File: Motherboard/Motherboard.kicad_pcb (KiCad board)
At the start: 2 copper layers, 75 x 75 mm, 43 parts, among them J1 AUX Analog A, J10 Moisture 4, J11 Moisture 5, J12 Power In, J2 AUX Analog B, J3 RPi 3B+, J4 AUX Digital A, J5 AUX Digital B, J6 Moisture 0, J7 Moisture 1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

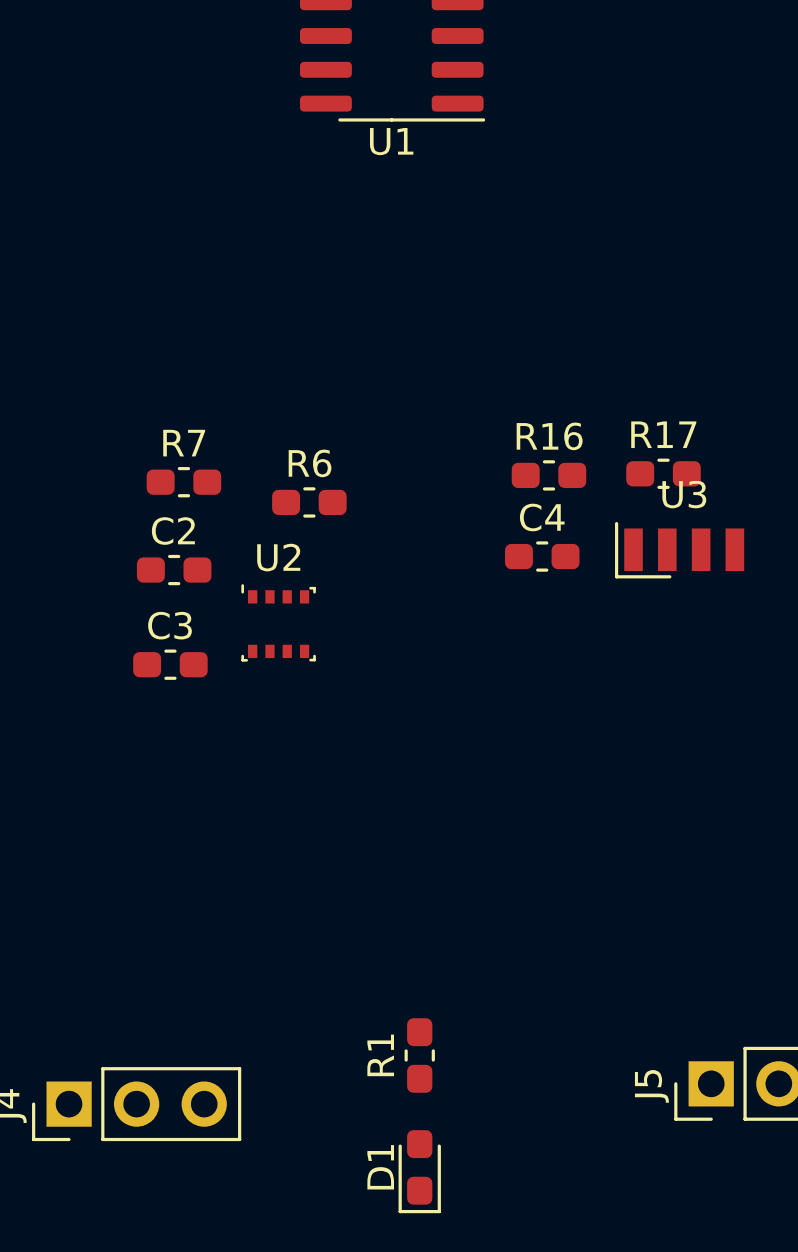
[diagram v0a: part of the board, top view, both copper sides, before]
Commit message: added missing footprint on new cap
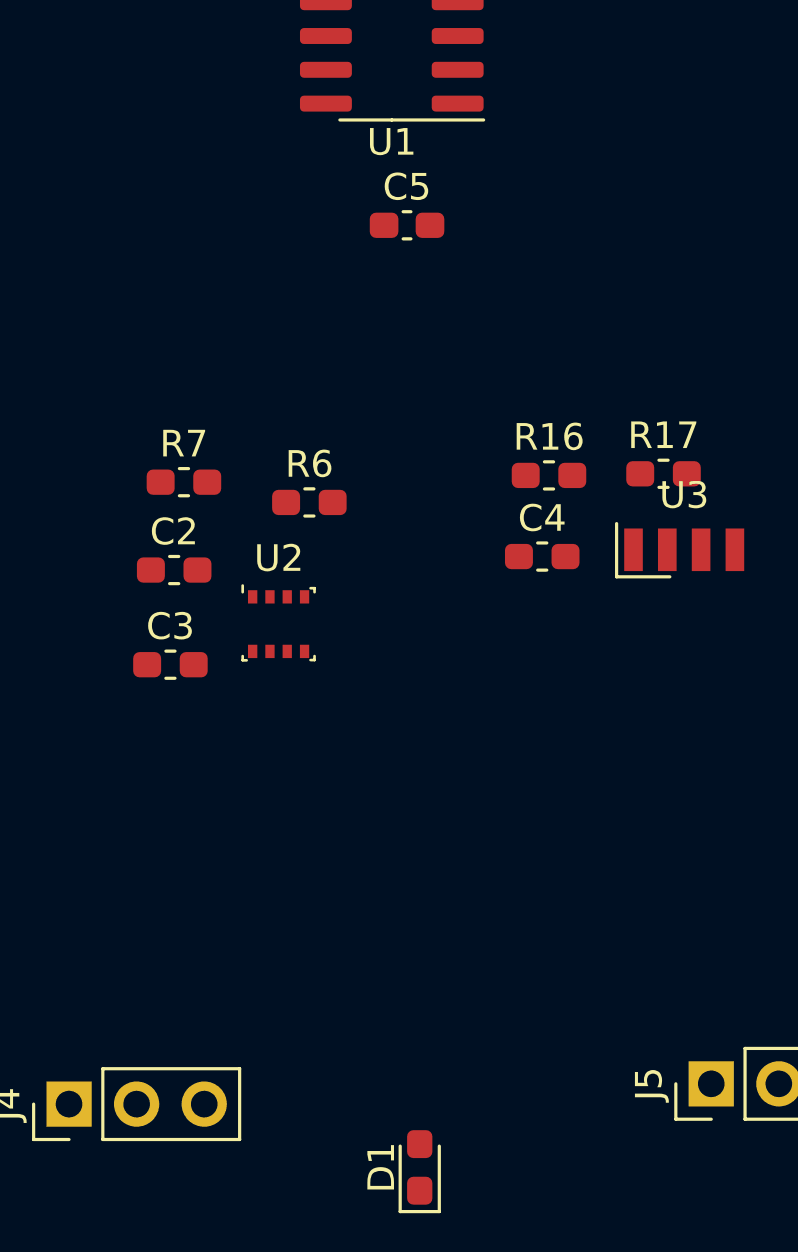
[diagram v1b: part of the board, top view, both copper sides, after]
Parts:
- removed R1: R, Resistor_SMD:R_0603_1608Metric_Pad1.05x0.95mm_HandSolder
- added C5: 1 uF, Capacitor_SMD:C_0603_1608Metric_Pad1.08x0.95mm_HandSolder, F.Cu at (81.3, 59.7)
- D1: value LED -> Blue 3.3V 20mA
- D2: value LED -> Green 2.2V 20mA
- R10, R12, R14, R2, R4, R8: value R -> 1.7 kohm
- R11, R13, R15, R3, R5, R9: value R -> 3.3 kohm
- R18: value R -> 150 ohm
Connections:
- D1 pad 2: Net-(D1-Pad2) -> GPIO_21
- J3 pad 12: GPIO_18-CLK -> (no net)
- J3 pad 23: (no net) -> GPIO_11-SCLK
- U1 pad 13: GPIO_18-CLK -> GPIO_11-SCLK

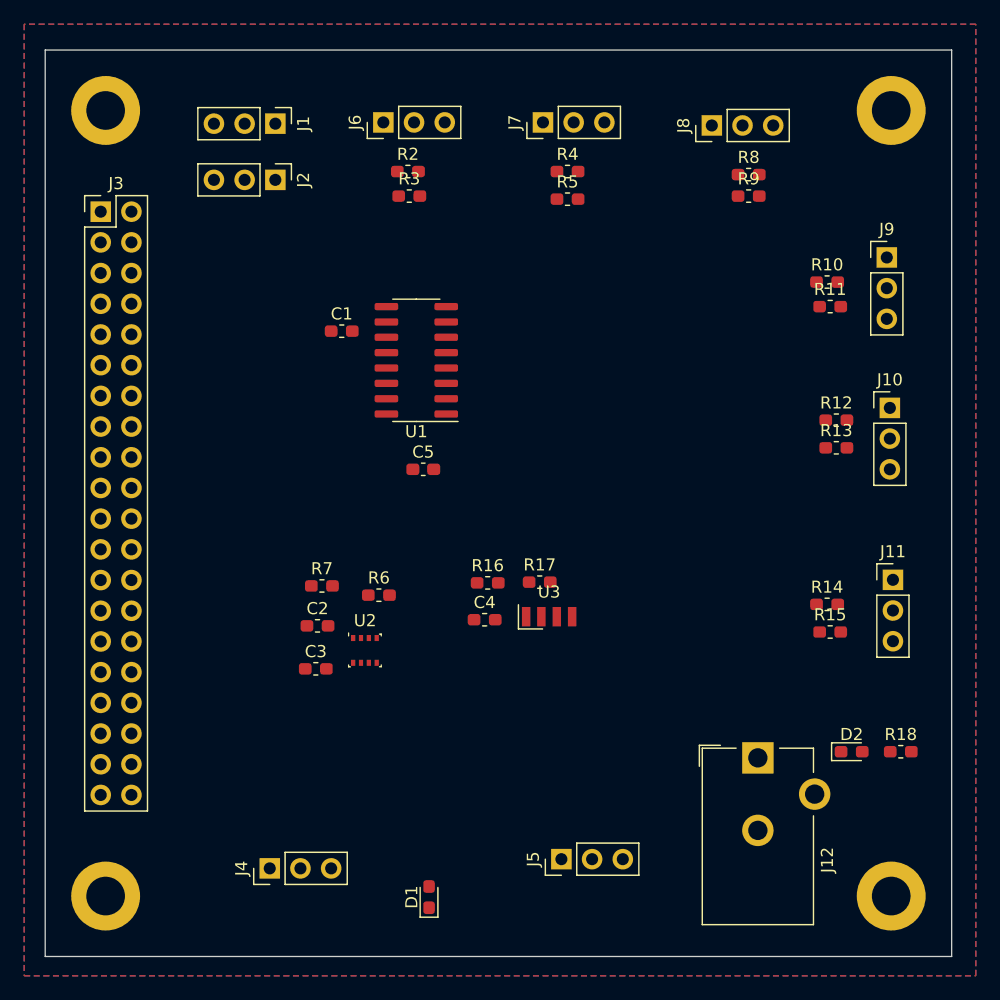
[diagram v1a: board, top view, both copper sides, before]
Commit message: Analog routed
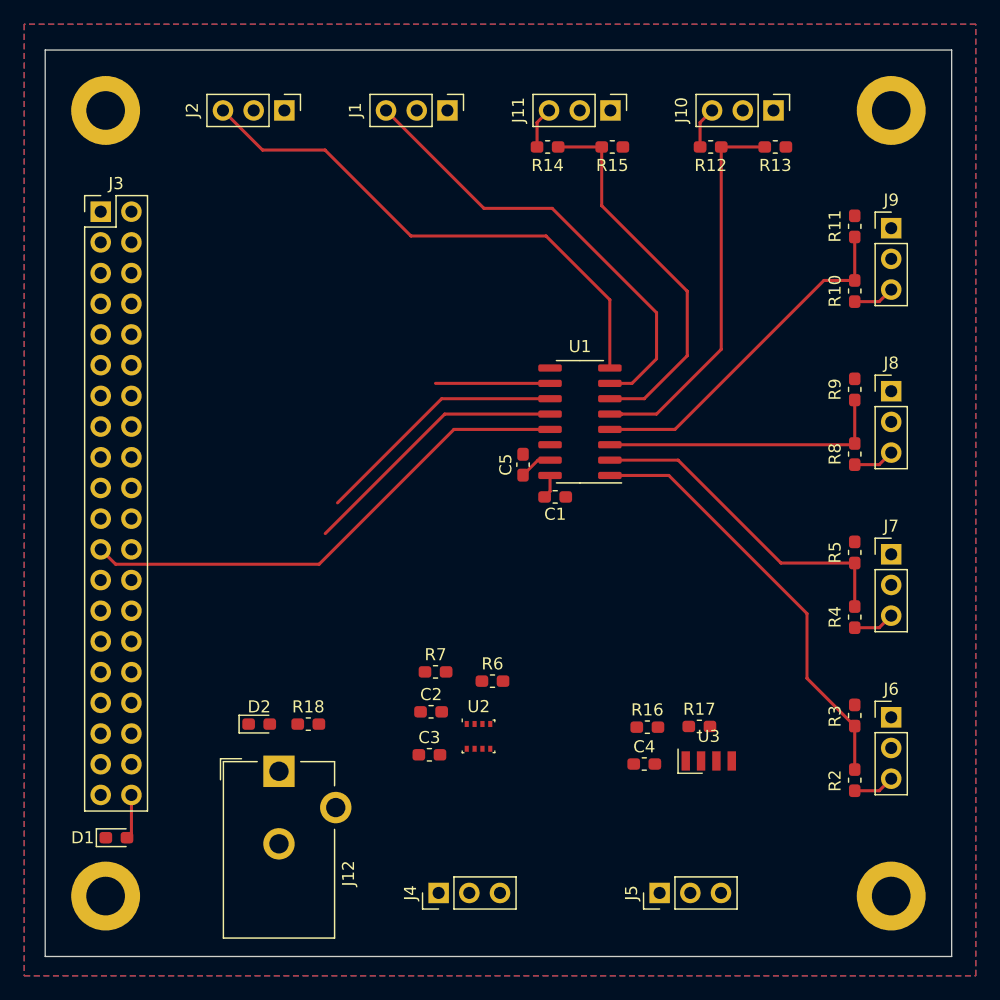
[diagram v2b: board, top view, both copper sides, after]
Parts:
- moved J6 64.7 mm to (120.0, 80.2), turned to 0 degrees
- moved R2 62.5 mm to (117.0, 85.4), turned to 90 degrees
- moved R3 56.6 mm to (117.0, 80.1), turned to 90 degrees
- moved D2 49.1 mm to (67.7, 80.8)
- moved R18 49.1 mm to (71.8, 80.8)
- moved J7 45.9 mm to (120.0, 66.7), turned to 0 degrees
- moved J11 45.3 mm to (96.8, 30.0), turned to 270 degrees
- moved R14 44.4 mm to (91.6, 33.0)
- moved R15 44.0 mm to (96.9, 33.0)
- moved R4 43.9 mm to (117.0, 71.9), turned to 90 degrees
- moved J12 39.6 mm to (69.3, 84.7)
- moved R5 37.7 mm to (117.0, 66.6), turned to 90 degrees
- moved J8 26.5 mm to (120.0, 53.2), turned to 0 degrees
- moved J10 26.4 mm to (110.3, 30.0), turned to 270 degrees
- moved D1 26.3 mm to (55.9, 90.2), turned to 0 degrees
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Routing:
- net A7: track 0.00 -> 44.1 mm
- net GPIO_11-SCLK: track 0.00 -> 42.3 mm
- net A6: track 0.00 -> 37.8 mm
- net A0: track 0.00 -> 35.6 mm
- net A4: track 0.00 -> 31.8 mm
- net A5: track 0.00 -> 31.7 mm
- net A3: track 0.00 -> 29.0 mm
- net A1: track 0.00 -> 27.4 mm
- net A2: track 0.00 -> 23.9 mm
- net GPIO_9-MISO: track 0.00 -> 22.7 mm
- net GPIO_10-MOSI: track 0.00 -> 21.2 mm
- net GPIO_8-CE0: track 0.00 -> 9.48 mm
- net +3V3: track 0.00 -> 4.71 mm
- net GPIO_21: track 0.00 -> 3.69 mm
- net Net-(J11-Pad3): track 0.00 -> 3.43 mm
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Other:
- net class Default: clearance 0.2 -> 0.254; trace_width 0.25 -> 0.254
- rule trace_clearance: 0.2 -> 0.254

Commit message: Routing complete
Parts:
- moved U3 41.7 mm to (86.9, 46.2), turned to 90 degrees
- moved C4 41.1 mm to (83.3, 46.3), turned to 180 degrees
- moved R16 40.1 mm to (83.3, 44.5), turned to 180 degrees
- moved R17 38.9 mm to (83.3, 48.1), turned to 180 degrees
- moved U2 38.8 mm to (70.3, 46.3)
- moved R6 37.5 mm to (70.4, 43.6), turned to 180 degrees
- moved C2 36.6 mm to (67.2, 46.3), turned to 90 degrees
- moved C3 36.1 mm to (70.4, 49.0)
- moved J5 33.4 mm to (67.4, 95.0)
- moved R7 31.4 mm to (73.4, 46.3), turned to 270 degrees
- moved J4 20.0 mm to (102.5, 95.0)
- moved R18 18.6 mm to (90.2, 78.1), turned to 180 degrees
- moved J12 17.5 mm to (86.8, 82.6)
- moved D2 16.0 mm to (83.4, 78.1)
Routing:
- net +3V3: track 4.71 -> 250.0 mm, vias 0 -> 1
- net +5V: track 0.00 -> 226.9 mm
- net D12: track 0.00 -> 58.2 mm
- net GPIO_3-SCL: track 0.00 -> 46.3 mm
- net GPIO_8-CE0: track 9.48 -> 52.2 mm
- net GPIO_2-SDA: track 0.00 -> 36.8 mm
- net D13: track 0.00 -> 24.5 mm
- net GPIO_10-MOSI: track 21.2 -> 40.2 mm
- net GPIO_9-MISO: track 22.7 -> 40.8 mm
- net Net-(D2-Pad2): track 0.00 -> 4.99 mm
- net +5VA: track 0.00 -> 2.54 mm
- net GND: vias 0 -> 8
